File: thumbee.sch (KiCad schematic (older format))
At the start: 60 parts, among them J11 Conn_02x05_Odd_Even, J12 USB_B, U1 msc313e, U2 spinor, U3 ht42b534-1, U4 RT8059GJ5, U5 RT8059GJ5, U6 RT8059GJ5, U7 xc6204xxxxMR, Y1 Crystal

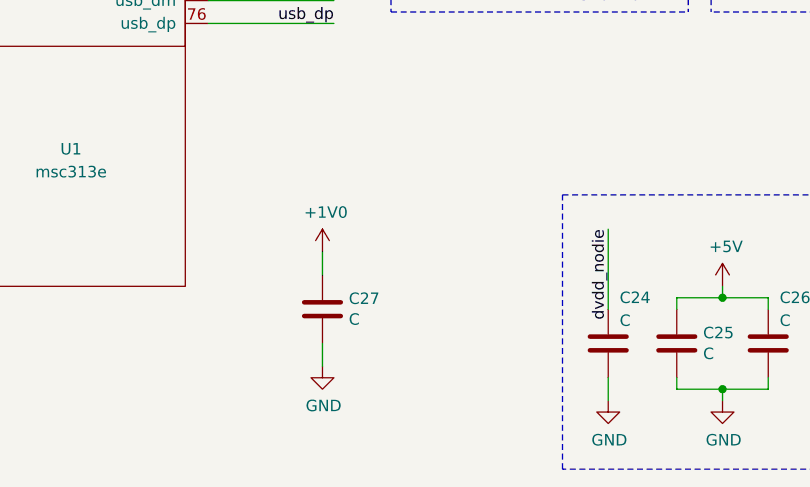
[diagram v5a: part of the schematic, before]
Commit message: Some clean up. Add some decoupling caps in the left over space.
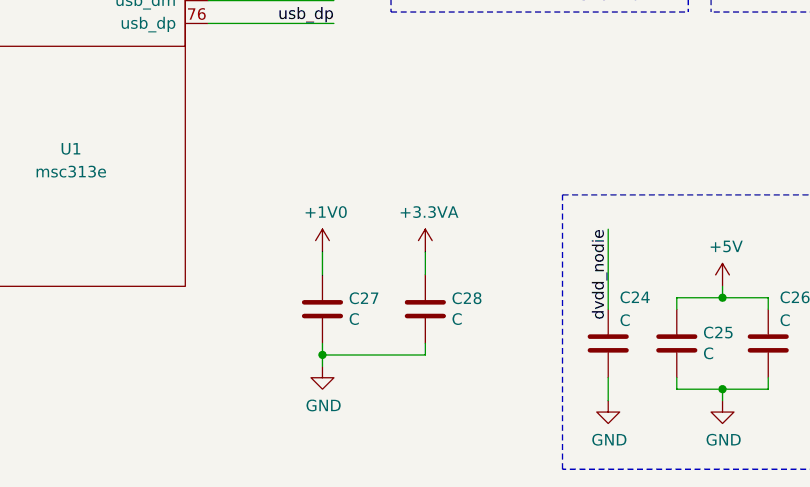
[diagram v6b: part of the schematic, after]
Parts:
- added C28: C, Capacitor_SMD:C_0603_1608Metric, symbol Device:C
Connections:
- net +3.3VA: now also C28.1
- net GND: now also C28.2
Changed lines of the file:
@@
 $EndComp
 Wire Wire Line
-	4050 7150 4050 7250
+	4050 7150 4050 7200
 Wire Wire Line
 	4050 6750 4050 6850
+$Comp
+L Device:C C28
+U 1 1 5D060C32
+P 4500 7000
+F 0 "C28" H 4615 7046 50  0000 L CNN
+F 1 "C" H 4615 6955 50  0000 L CNN
+F 2 "Capacitor_SMD:C_0603_1608Metric" H 4538 6850 50  0001 C CNN
+F 3 "~" H 4500 7000 50  0001 C CNN
+	1    4500 7000
+	1    0    0    -1
+$EndComp
+$Comp
+L power:+3.3VA #PWR03
+U 1 1 5D060D8B
+P 4500 6750
+F 0 "#PWR03" H 4500 6600 50  0001 C CNN
+F 1 "+3.3VA" H 4515 6923 50  0000 C CNN
+F 2 "" H 4500 6750 50  0001 C CNN
+F 3 "" H 4500 6750 50  0001 C CNN
+	1    4500 6750
+	1    0    0    -1
+$EndComp
+Wire Wire Line
+	4500 6750 4500 6850
+Wire Wire Line
+	4500 7150 4500 7200
+Wire Wire Line
+	4500 7200 4050 7200
+Connection ~ 4050 7200
+Wire Wire Line
+	4050 7200 4050 7250
 $EndSCHEMATC

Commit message: Rev0
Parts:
- added C29, C30, C31, C32: C, Capacitor_SMD:C_0603_1608Metric, symbol Device:C
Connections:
- net +1V8: now also C31.1, C32.1
- net +3V3: now also C29.1, C30.1
- net GND: now also C29.2, C30.2, C31.2, C32.2
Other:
- moved on the sheet: C27, C28
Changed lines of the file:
@@
 L Device:C C27
 U 1 1 5CBCB6E8
-P 4050 7000
-F 0 "C27" H 4165 7046 50  0000 L CNN
-F 1 "C" H 4165 6955 50  0000 L CNN
-F 2 "Capacitor_SMD:C_0603_1608Metric" H 4088 6850 50  0001 C CNN
-F 3 "~" H 4050 7000 50  0001 C CNN
-	1    4050 7000
+P -2650 7000
+F 0 "C27" H -2535 7046 50  0000 L CNN
+F 1 "C" H -2535 6955 50  0000 L CNN
+F 2 "Capacitor_SMD:C_0603_1608Metric" H -2612 6850 50  0001 C CNN
+F 3 "~" H -2650 7000 50  0001 C CNN
+	1    -2650 7000
 	1    0    0    -1
 $EndComp
@@
 L power:+1V0 #PWR01
 U 1 1 5CBCB9D7
-P 4050 6750
-F 0 "#PWR01" H 4050 6600 50  0001 C CNN
-F 1 "+1V0" H 4065 6923 50  0000 C CNN
-F 2 "" H 4050 6750 50  0001 C CNN
-F 3 "" H 4050 6750 50  0001 C CNN
-	1    4050 6750
+P -2650 6750
+F 0 "#PWR01" H -2650 6600 50  0001 C CNN
+F 1 "+1V0" H -2635 6923 50  0000 C CNN
+F 2 "" H -2650 6750 50  0001 C CNN
+F 3 "" H -2650 6750 50  0001 C CNN
+	1    -2650 6750
 	1    0    0    -1
 $EndComp
@@
 L power:GND #PWR02
 U 1 1 5CCC1EDA
-P 4050 7250
-F 0 "#PWR02" H 4050 7000 50  0001 C CNN
-F 1 "GND" H 4055 7077 50  0000 C CNN
-F 2 "" H 4050 7250 50  0001 C CNN
-F 3 "" H 4050 7250 50  0001 C CNN
-	1    4050 7250
+P -2650 7250
+F 0 "#PWR02" H -2650 7000 50  0001 C CNN
+F 1 "GND" H -2645 7077 50  0000 C CNN
+F 2 "" H -2650 7250 50  0001 C CNN
+F 3 "" H -2650 7250 50  0001 C CNN
+	1    -2650 7250
 	1    0    0    -1
 $EndComp
 Wire Wire Line
-	4050 7150 4050 7200
+	-2650 7150 -2650 7200
 Wire Wire Line
-	4050 6750 4050 6850
+	-2650 6750 -2650 6850
 $Comp
 L Device:C C28
 U 1 1 5D060C32
-P 4500 7000
-F 0 "C28" H 4615 7046 50  0000 L CNN
-F 1 "C" H 4615 6955 50  0000 L CNN
-F 2 "Capacitor_SMD:C_0603_1608Metric" H 4538 6850 50  0001 C CNN
-F 3 "~" H 4500 7000 50  0001 C CNN
-	1    4500 7000
+P -2200 7000
+F 0 "C28" H -2085 7046 50  0000 L CNN
+F 1 "C" H -2085 6955 50  0000 L CNN
+F 2 "Capacitor_SMD:C_0603_1608Metric" H -2162 6850 50  0001 C CNN
+F 3 "~" H -2200 7000 50  0001 C CNN
+	1    -2200 7000
 	1    0    0    -1
 $EndComp
@@
 L power:+3.3VA #PWR03
 U 1 1 5D060D8B
-P 4500 6750
-F 0 "#PWR03" H 4500 6600 50  0001 C CNN
-F 1 "+3.3VA" H 4515 6923 50  0000 C CNN
-F 2 "" H 4500 6750 50  0001 C CNN
-F 3 "" H 4500 6750 50  0001 C CNN
-	1    4500 6750
+P -2200 6750
+F 0 "#PWR03" H -2200 6600 50  0001 C CNN
+F 1 "+3.3VA" H -2185 6923 50  0000 C CNN
+F 2 "" H -2200 6750 50  0001 C CNN
+F 3 "" H -2200 6750 50  0001 C CNN
+	1    -2200 6750
 	1    0    0    -1
 $EndComp
 Wire Wire Line
-	4500 6750 4500 6850
+	-2200 6750 -2200 6850
 Wire Wire Line
-	4500 7150 4500 7200
+	-2200 7150 -2200 7200
 Wire Wire Line
-	4500 7200 4050 7200
-Connection ~ 4050 7200
+	-2200 7200 -2650 7200
+Connection ~ -2650 7200
 Wire Wire Line
-	4050 7200 4050 7250
+	-2650 7200 -2650 7250
+$Comp
+L Device:C C29
+U 1 1 5C73DDFC
+P -1800 7000
+F 0 "C29" H -1685 7046 50  0000 L CNN
+F 1 "C" H -1685 6955 50  0000 L CNN
+F 2 "Capacitor_SMD:C_0603_1608Metric" H -1762 6850 50  0001 C CNN
+F 3 "~" H -1800 7000 50  0001 C CNN
+	1    -1800 7000
+	1    0    0    -1
+$EndComp
+$Comp
+L power:+3.3V #PWR04
+U 1 1 5C73DF13
+P -1800 6750
+F 0 "#PWR04" H -1800 6600 50  0001 C CNN
+F 1 "+3.3V" H -1785 6923 50  0000 C CNN
+F 2 "" H -1800 6750 50  0001 C CNN
+F 3 "" H -1800 6750 50  0001 C CNN
+	1    -1800 6750
+	1    0    0    -1
+$EndComp
+Wire Wire Line
+	-1800 6750 -1800 6800
+Wire Wire Line
+	-1800 7150 -1800 7200
+Wire Wire Line
+	-1800 7200 -2200 7200
+Connection ~ -2200 7200
+$Comp
+L Device:C C30
+U 1 1 5C7FA26E
+P -1400 7000
+F 0 "C30" H -1285 7046 50  0000 L CNN
+F 1 "C" H -1285 6955 50  0000 L CNN
+F 2 "Capacitor_SMD:C_0603_1608Metric" H -1362 6850 50  0001 C CNN
+F 3 "~" H -1400 7000 50  0001 C CNN
+	1    -1400 7000
+	1    0    0    -1
+$EndComp
+Wire Wire Line
+	-1800 6800 -1400 6800
+Wire Wire Line
+	-1400 6800 -1400 6850
+Connection ~ -1800 6800
+Wire Wire Line
+	-1800 6800 -1800 6850
+Wire Wire Line
+	-1400 7150 -1400 7200
+Wire Wire Line
+	-1400 7200 -1800 7200
+Connection ~ -1800 7200
+$Comp
+L Device:C C31
+U 1 1 5C8BA434
+P -1000 7000
+F 0 "C31" H -885 7046 50  0000 L CNN
+F 1 "C" H -885 6955 50  0000 L CNN
+F 2 "Capacitor_SMD:C_0603_1608Metric" H -962 6850 50  0001 C CNN
+F 3 "~" H -1000 7000 50  0001 C CNN
+	1    -1000 7000
+	1    0    0    -1
+$EndComp
+$Comp
+L Device:C C32
+U 1 1 5C8BA557
+P -700 7000
+F 0 "C32" H -585 7046 50  0000 L CNN
+F 1 "C" H -585 6955 50  0000 L CNN
+F 2 "Capacitor_SMD:C_0603_1608Metric" H -662 6850 50  0001 C CNN
+F 3 "~" H -700 7000 50  0001 C CNN
+	1    -700 7000
+	1    0    0    -1
+$EndComp
+Wire Wire Line
+	-700 7150 -700 7200
+Wire Wire Line
+	-700 7200 -1000 7200
+Connection ~ -1400 7200
+Wire Wire Line
+	-1000 7150 -1000 7200
+Connection ~ -1000 7200
+Wire Wire Line
+	-1000 7200 -1400 7200
+Wire Wire Line
+	-700 6850 -700 6800
+Wire Wire Line
+	-700 6800 -1000 6800
+Wire Wire Line
+	-1000 6800 -1000 6850
+Wire Wire Line
+	-1000 6800 -1000 6750
+Connection ~ -1000 6800
+$Comp
+L power:+1V8 #PWR05
+U 1 1 5C9C1705
+P -1000 6750
+F 0 "#PWR05" H -1000 6600 50  0001 C CNN
+F 1 "+1V8" H -985 6923 50  0000 C CNN
+F 2 "" H -1000 6750 50  0001 C CNN
+F 3 "" H -1000 6750 50  0001 C CNN
+	1    -1000 6750
+	1    0    0    -1
+$EndComp
 $EndSCHEMATC

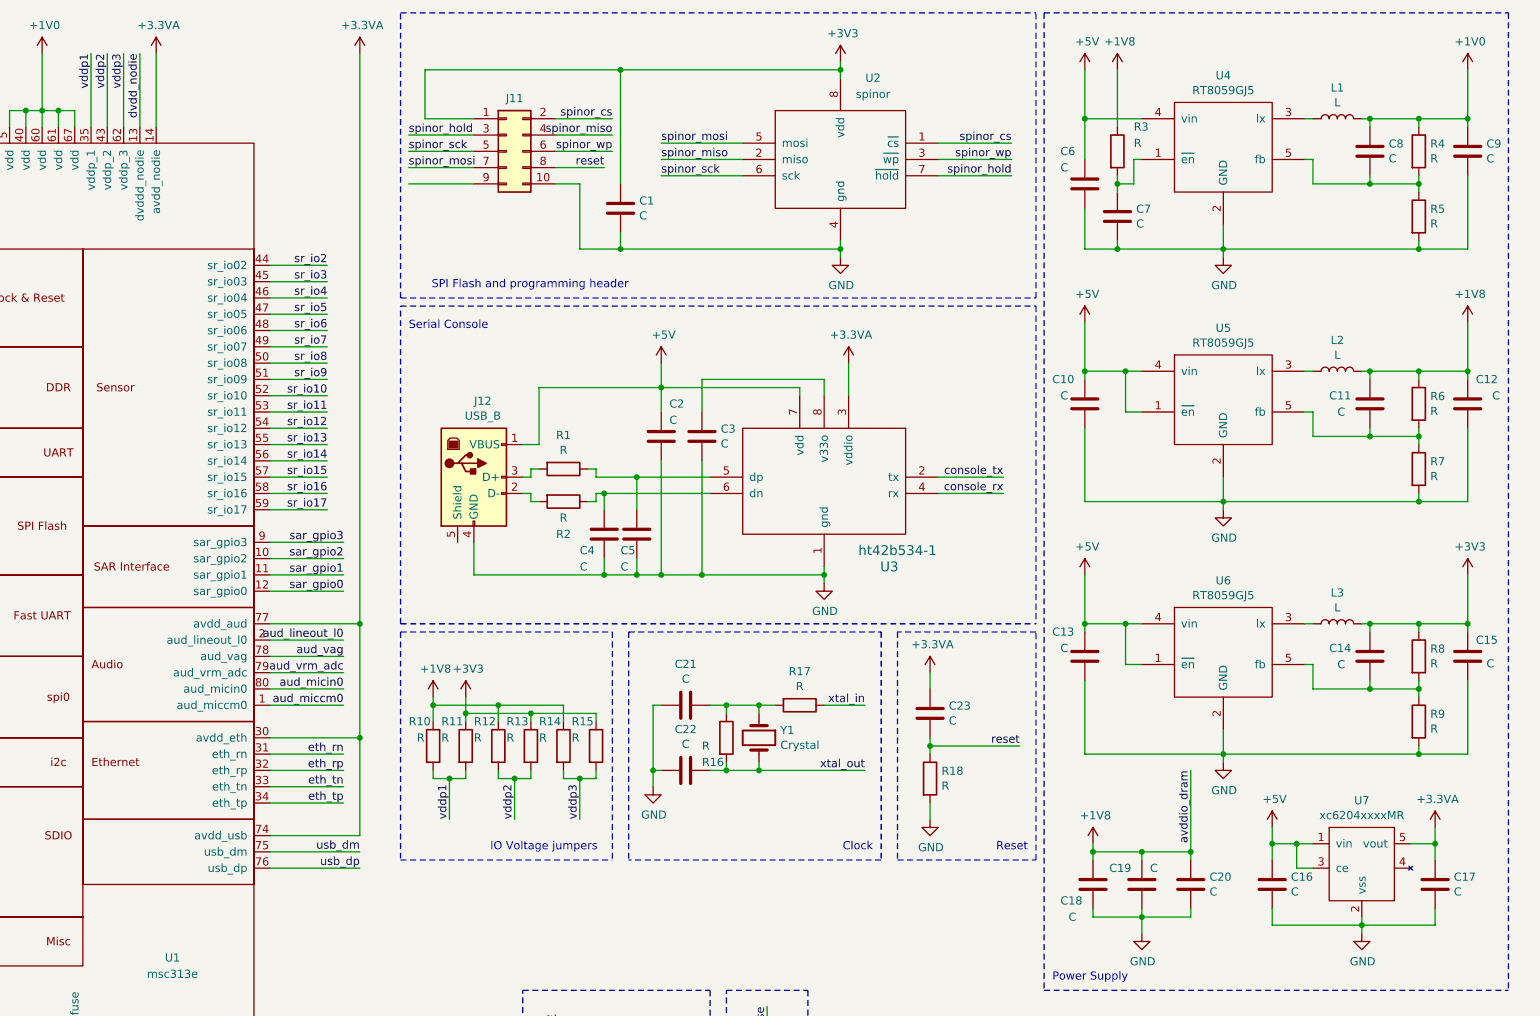
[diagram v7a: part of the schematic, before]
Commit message: Add some component values. Fix avdd_nodie and dvdd_nodie.
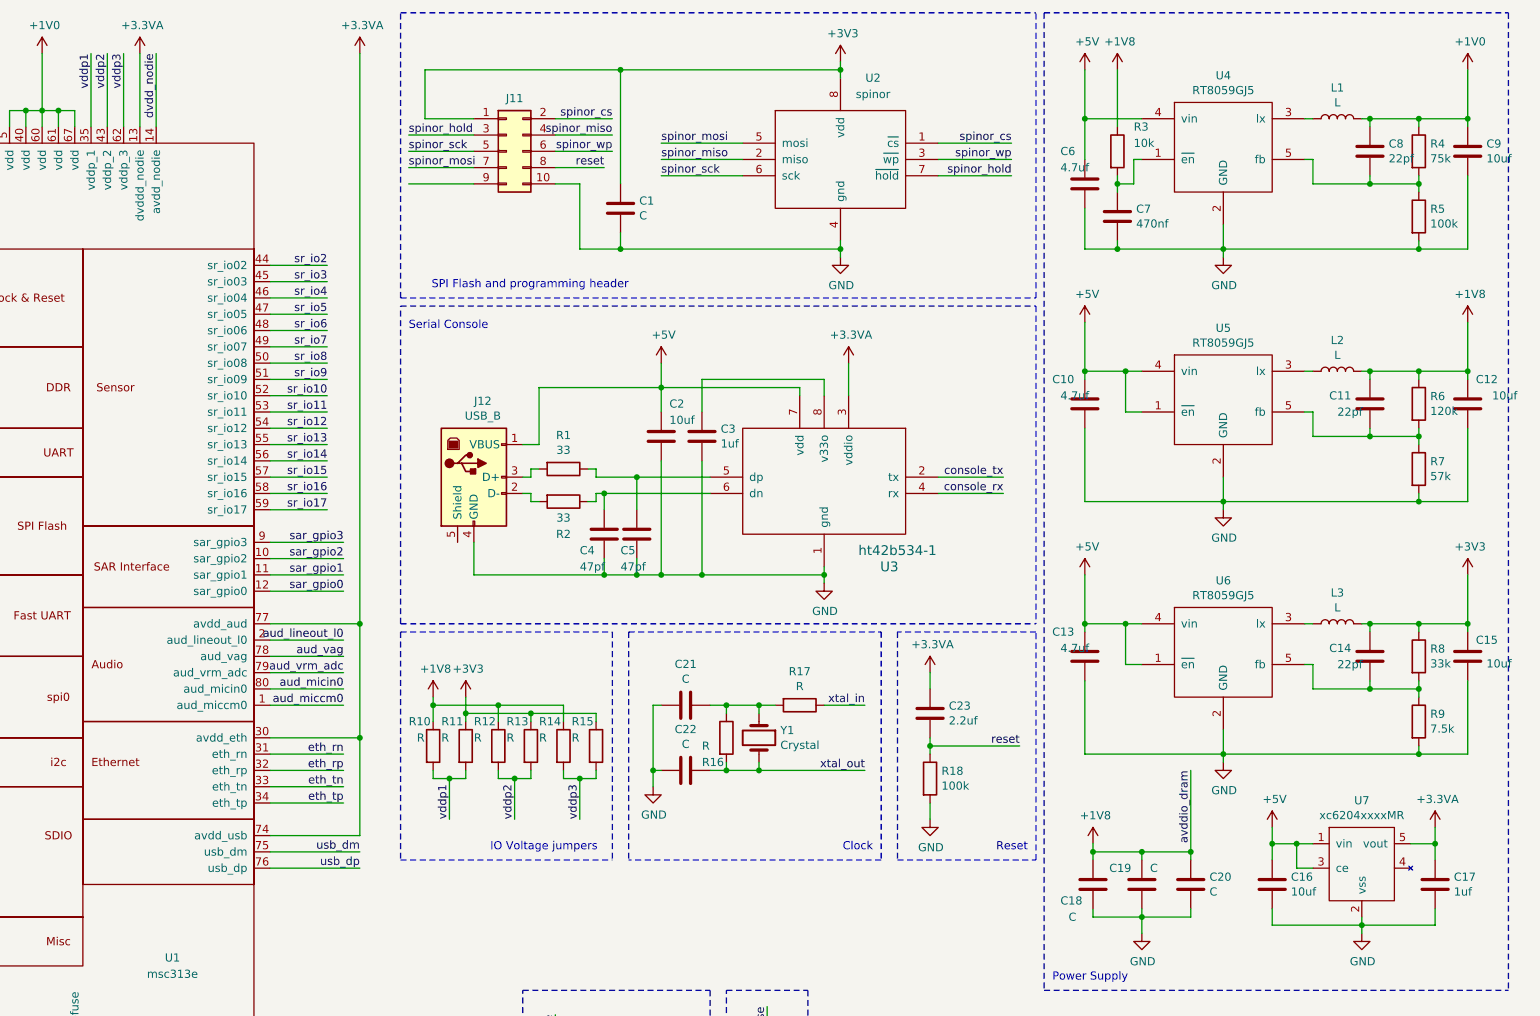
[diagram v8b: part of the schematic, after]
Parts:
- C10, C13, C6: value C -> 4.7uf
- C11, C14, C8: value C -> 22pf
- C12, C15, C16, C2, C9: value C -> 10uf
- C17, C3: value C -> 1uf
- C23: value C -> 2.2uf
- C4, C5: value C -> 47pf
- C7: value C -> 470nf
- R1, R2: value R -> 33
- R18, R5: value R -> 100k
- R3: value R -> 10k
- R4: value R -> 75k
- R6: value R -> 120k
- R7: value R -> 57k
- R8: value R -> 33k
- R9: value R -> 7.5k
- U1: footprint s2qfn80:QFN-80_EP_8x8_Pitch0.35mm -> (none)
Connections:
- net +3.3VA: now also U1.13 (dvddd_nodie); no longer U1.14 (avdd_nodie)
- net dvdd_nodie: now also U1.14 (avdd_nodie); no longer U1.13 (dvddd_nodie)
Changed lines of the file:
@@
 F 0 "U1" H 2950 1300 50  0000 C CNN
 F 1 "msc313e" H 2950 1200 50  0000 C CNN
-F 2 "s2qfn80:QFN-80_EP_8x8_Pitch0.35mm" H 1200 5450 50  0001 C CNN
+F 2 "" H 1200 5450 50  0001 C CNN
 F 3 "" H 1200 5450 50  0001 C CNN
 	1    2400 3800
@@
 P 7600 4800
 F 0 "C23" H 7715 4846 50  0000 L CNN
-F 1 "C" H 7715 4755 50  0000 L CNN
+F 1 "2.2uf" H 7715 4755 50  0000 L CNN
 F 2 "Capacitor_SMD:C_0603_1608Metric" H 7638 4650 50  0001 C CNN
 F 3 "~" H 7600 4800 50  0001 C CNN
@@
 P 7600 5200
 F 0 "R18" H 7670 5246 50  0000 L CNN
-F 1 "R" H 7670 5155 50  0000 L CNN
+F 1 "100k" H 7670 5155 50  0000 L CNN
 F 2 "Resistor_SMD:R_0603_1608Metric" V 7530 5200 50  0001 C CNN
 F 3 "~" H 7600 5200 50  0001 C CNN
@@
 L power:+3.3VA #PWR0107
 U 1 1 5C4EEA93
-P 2850 750
-F 0 "#PWR0107" H 2850 600 50  0001 C CNN
-F 1 "+3.3VA" H 2865 923 50  0000 C CNN
-F 2 "" H 2850 750 50  0001 C CNN
-F 3 "" H 2850 750 50  0001 C CNN
-	1    2850 750
+P 2750 750
+F 0 "#PWR0107" H 2750 600 50  0001 C CNN
+F 1 "+3.3VA" H 2765 923 50  0000 C CNN
+F 2 "" H 2750 750 50  0001 C CNN
+F 3 "" H 2750 750 50  0001 C CNN
+	1    2750 750
 	1    0    0    -1
 $EndComp
@@
 P 10900 1350
 F 0 "C9" H 11015 1396 50  0000 L CNN
-F 1 "C" H 11015 1305 50  0000 L CNN
+F 1 "10uf" H 11015 1305 50  0000 L CNN
 F 2 "Capacitor_SMD:C_0603_1608Metric" H 10938 1200 50  0001 C CNN
 F 3 "~" H 10900 1350 50  0001 C CNN
@@
 P 10600 1350
 F 0 "R4" H 10670 1396 50  0000 L CNN
-F 1 "R" H 10670 1305 50  0000 L CNN
+F 1 "75k" H 10670 1305 50  0000 L CNN
 F 2 "Resistor_SMD:R_0603_1608Metric" V 10530 1350 50  0001 C CNN
 F 3 "~" H 10600 1350 50  0001 C CNN
@@
 P 10600 1750
 F 0 "R5" H 10670 1796 50  0000 L CNN
-F 1 "R" H 10670 1705 50  0000 L CNN
+F 1 "100k" H 10670 1705 50  0000 L CNN
 F 2 "Resistor_SMD:R_0603_1608Metric" V 10530 1750 50  0001 C CNN
 F 3 "~" H 10600 1750 50  0001 C CNN
@@
 P 8550 1550
 F 0 "C6" H 8400 1750 50  0000 L CNN
-F 1 "C" H 8400 1650 50  0000 L CNN
+F 1 "4.7uf" H 8400 1650 50  0000 L CNN
 F 2 "Capacitor_SMD:C_0603_1608Metric" H 8588 1400 50  0001 C CNN
 F 3 "~" H 8550 1550 50  0001 C CNN
@@
 P 10300 1350
 F 0 "C8" H 10415 1396 50  0000 L CNN
-F 1 "C" H 10415 1305 50  0000 L CNN
+F 1 "22pf" H 10415 1305 50  0000 L CNN
 F 2 "Capacitor_SMD:C_0603_1608Metric" H 10338 1200 50  0001 C CNN
 F 3 "~" H 10300 1350 50  0001 C CNN
@@
 P 10900 2900
 F 0 "C12" H 10950 3050 50  0000 L CNN
-F 1 "C" H 11050 2950 50  0000 L CNN
+F 1 "10uf" H 11050 2950 50  0000 L CNN
 F 2 "Capacitor_SMD:C_0603_1608Metric" H 10938 2750 50  0001 C CNN
 F 3 "~" H 10900 2900 50  0001 C CNN
@@
 P 10600 2900
 F 0 "R6" H 10670 2946 50  0000 L CNN
-F 1 "R" H 10670 2855 50  0000 L CNN
+F 1 "120k" H 10670 2855 50  0000 L CNN
 F 2 "Resistor_SMD:R_0603_1608Metric" V 10530 2900 50  0001 C CNN
 F 3 "~" H 10600 2900 50  0001 C CNN
@@
 P 10600 3300
 F 0 "R7" H 10670 3346 50  0000 L CNN
-F 1 "R" H 10670 3255 50  0000 L CNN
+F 1 "57k" H 10670 3255 50  0000 L CNN
 F 2 "Resistor_SMD:R_0603_1608Metric" V 10530 3300 50  0001 C CNN
 F 3 "~" H 10600 3300 50  0001 C CNN
@@
 P 8550 2900
 F 0 "C10" H 8350 3050 50  0000 L CNN
-F 1 "C" H 8400 2950 50  0000 L CNN
+F 1 "4.7uf" H 8400 2950 50  0000 L CNN
 F 2 "Capacitor_SMD:C_0603_1608Metric" H 8588 2750 50  0001 C CNN
 F 3 "~" H 8550 2900 50  0001 C CNN
@@
 P 10300 2900
 F 0 "C11" H 10050 2950 50  0000 L CNN
-F 1 "C" H 10100 2850 50  0000 L CNN
+F 1 "22pf" H 10100 2850 50  0000 L CNN
 F 2 "Capacitor_SMD:C_0603_1608Metric" H 10338 2750 50  0001 C CNN
 F 3 "~" H 10300 2900 50  0001 C CNN
@@
 P 10900 4450
 F 0 "C15" H 10950 4550 50  0000 L CNN
-F 1 "C" H 11015 4405 50  0000 L CNN
+F 1 "10uf" H 11015 4405 50  0000 L CNN
 F 2 "Capacitor_SMD:C_0603_1608Metric" H 10938 4300 50  0001 C CNN
 F 3 "~" H 10900 4450 50  0001 C CNN
@@
 P 10600 4450
 F 0 "R8" H 10670 4496 50  0000 L CNN
-F 1 "R" H 10670 4405 50  0000 L CNN
+F 1 "33k" H 10670 4405 50  0000 L CNN
 F 2 "Resistor_SMD:R_0603_1608Metric" V 10530 4450 50  0001 C CNN
 F 3 "~" H 10600 4450 50  0001 C CNN
@@
 P 10600 4850
 F 0 "R9" H 10670 4896 50  0000 L CNN
-F 1 "R" H 10670 4805 50  0000 L CNN
+F 1 "7.5k" H 10670 4805 50  0000 L CNN
 F 2 "Resistor_SMD:R_0603_1608Metric" V 10530 4850 50  0001 C CNN
 F 3 "~" H 10600 4850 50  0001 C CNN
@@
 P 8550 4450
 F 0 "C13" H 8350 4600 50  0000 L CNN
-F 1 "C" H 8400 4500 50  0000 L CNN
+F 1 "4.7uf" H 8400 4500 50  0000 L CNN
 F 2 "Capacitor_SMD:C_0603_1608Metric" H 8588 4300 50  0001 C CNN
 F 3 "~" H 8550 4450 50  0001 C CNN
@@
 P 10300 4450
 F 0 "C14" H 10050 4500 50  0000 L CNN
-F 1 "C" H 10100 4400 50  0000 L CNN
+F 1 "22pf" H 10100 4400 50  0000 L CNN
 F 2 "Capacitor_SMD:C_0603_1608Metric" H 10338 4300 50  0001 C CNN
 F 3 "~" H 10300 4450 50  0001 C CNN
@@
 P 10700 5850
 F 0 "C17" H 10815 5896 50  0000 L CNN
-F 1 "C" H 10815 5805 50  0000 L CNN
+F 1 "1uf" H 10815 5805 50  0000 L CNN
 F 2 "Capacitor_SMD:C_0603_1608Metric" H 10738 5700 50  0001 C CNN
 F 3 "~" H 10700 5850 50  0001 C CNN
@@
 P 9700 5850
 F 0 "C16" H 9815 5896 50  0000 L CNN
-F 1 "C" H 9815 5805 50  0000 L CNN
+F 1 "10uf" H 9815 5805 50  0000 L CNN
 F 2 "Capacitor_SMD:C_0603_1608Metric" H 9738 5700 50  0001 C CNN
 F 3 "~" H 9700 5850 50  0001 C CNN
@@
 P 5350 3300
 F 0 "R1" V 5143 3300 50  0000 C CNN
-F 1 "R" V 5234 3300 50  0000 C CNN
+F 1 "33" V 5234 3300 50  0000 C CNN
 F 2 "Resistor_SMD:R_0603_1608Metric" V 5280 3300 50  0001 C CNN
 F 3 "~" H 5350 3300 50  0001 C CNN
@@
 P 5350 3500
 F 0 "R2" V 5550 3500 50  0000 C CNN
-F 1 "R" V 5450 3500 50  0000 C CNN
+F 1 "33" V 5450 3500 50  0000 C CNN
 F 2 "Resistor_SMD:R_0603_1608Metric" V 5280 3500 50  0001 C CNN
 F 3 "~" H 5350 3500 50  0001 C CNN
@@
 P 5800 3700
 F 0 "C5" H 5700 3600 50  0000 L CNN
-F 1 "C" H 5700 3500 50  0000 L CNN
+F 1 "47pf" H 5700 3500 50  0000 L CNN
 F 2 "Capacitor_SMD:C_0603_1608Metric" H 5838 3550 50  0001 C CNN
 F 3 "~" H 5800 3700 50  0001 C CNN
@@
 P 5600 3700
 F 0 "C4" H 5450 3600 50  0000 L CNN
-F 1 "C" H 5450 3500 50  0000 L CNN
+F 1 "47pf" H 5450 3500 50  0000 L CNN
 F 2 "Capacitor_SMD:C_0603_1608Metric" H 5638 3550 50  0001 C CNN
 F 3 "~" H 5600 3700 50  0001 C CNN
@@
 P 5950 3100
 F 0 "C2" H 6000 3300 50  0000 L CNN
-F 1 "C" H 6000 3200 50  0000 L CNN
+F 1 "10uf" H 6000 3200 50  0000 L CNN
 F 2 "Capacitor_SMD:C_0603_1608Metric" H 5988 2950 50  0001 C CNN
 F 3 "~" H 5950 3100 50  0001 C CNN
@@
 P 6200 3100
 F 0 "C3" H 6315 3146 50  0000 L CNN
-F 1 "C" H 6315 3055 50  0000 L CNN
+F 1 "1uf" H 6315 3055 50  0000 L CNN
 F 2 "Capacitor_SMD:C_0603_1608Metric" H 6238 2950 50  0001 C CNN
 F 3 "~" H 6200 3100 50  0001 C CNN
@@
 P 8750 1750
 F 0 "C7" H 8865 1796 50  0000 L CNN
-F 1 "C" H 8865 1705 50  0000 L CNN
+F 1 "470nf" H 8865 1705 50  0000 L CNN
 F 2 "Capacitor_SMD:C_0603_1608Metric" H 8788 1600 50  0001 C CNN
 F 3 "~" H 8750 1750 50  0001 C CNN
@@
 P 8750 1350
 F 0 "R3" H 8850 1500 50  0000 L CNN
-F 1 "R" H 8850 1400 50  0000 L CNN
+F 1 "10k" H 8850 1400 50  0000 L CNN
 F 2 "Resistor_SMD:R_0603_1608Metric" V 8680 1350 50  0001 C CNN
 F 3 "~" H 8750 1350 50  0001 C CNN
@@
 Wire Wire Line
 	5300 7300 5300 7400
-Text Label 2750 750  3    50   ~ 0
+Text Label 2850 750  3    50   ~ 0
 dvdd_nodie
 Wire Wire Line
